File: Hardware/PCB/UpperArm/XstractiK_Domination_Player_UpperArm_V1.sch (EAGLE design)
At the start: 57 parts, among them J1 USB4110-GF-A_REVB, Q1 MMBT2222, Q2 AO3401A, Q5 MMBT2222, Q6 MMBT2222, U1 ESP32-DEVKITC-32U, U2 RFM95W-915S2, U3 MCP73831T, U4 AP2112K-3.3, U5 MAX17048G, U6 ESP32-WROOM-32D, U7 CH340C, U8 DS3231SN, U9 QMC5883GY-271

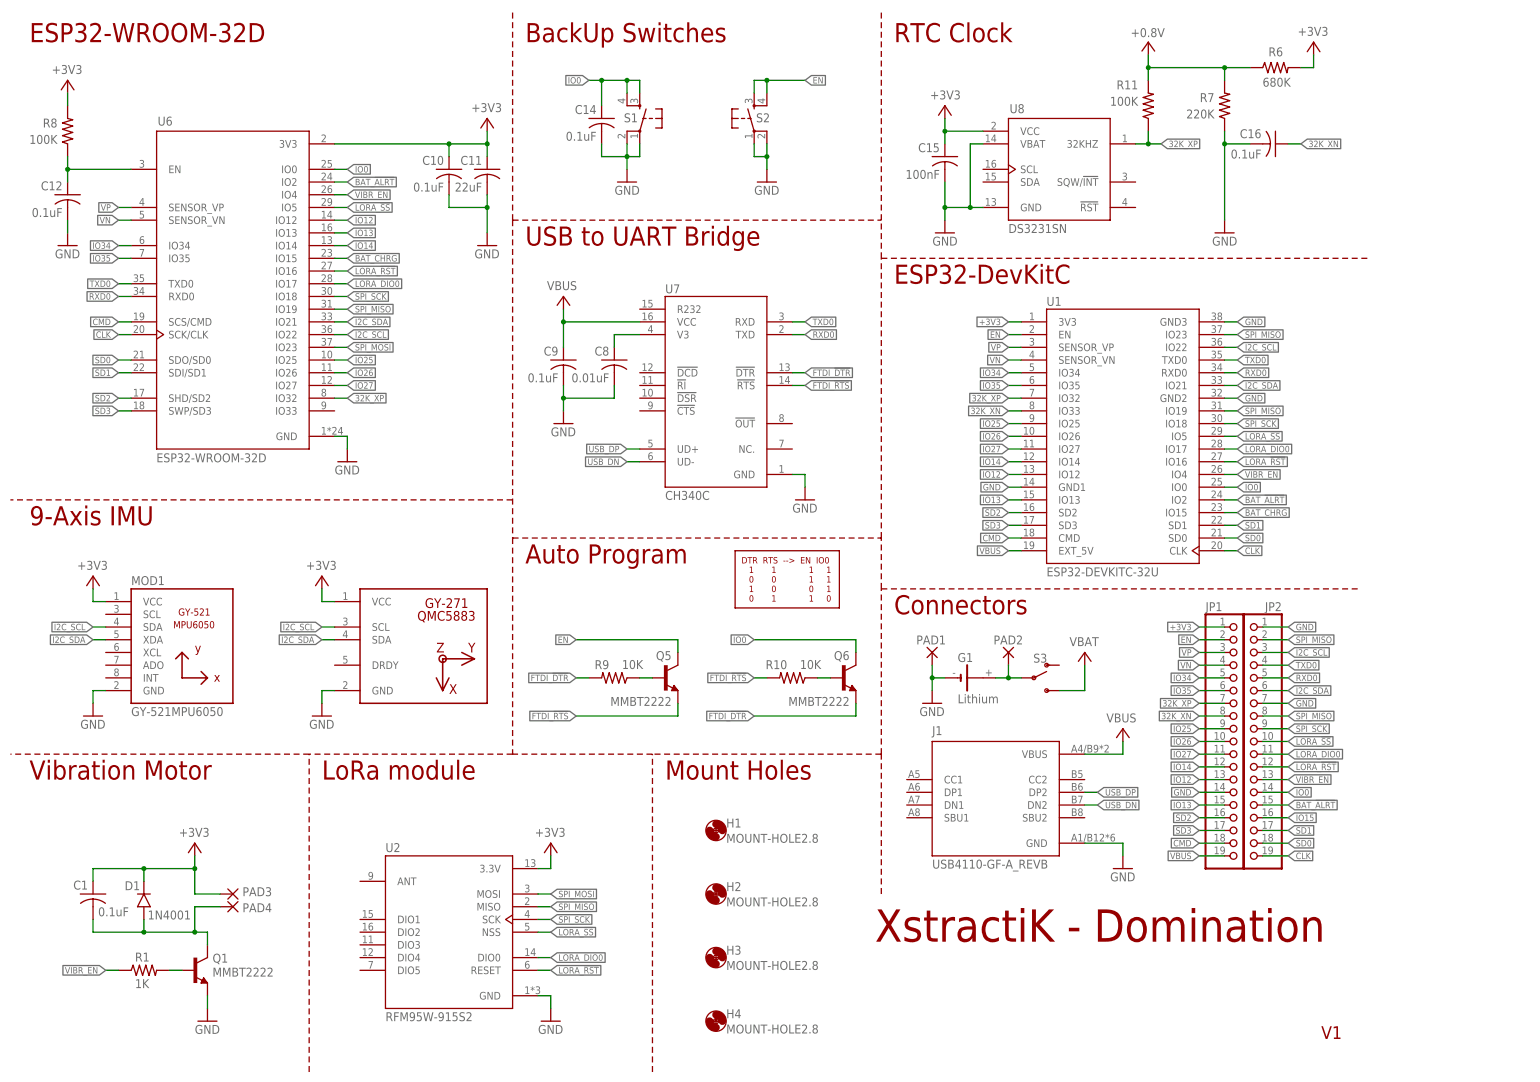
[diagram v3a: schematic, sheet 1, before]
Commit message: Schematic and PCB
UpperArm and Forearm designs
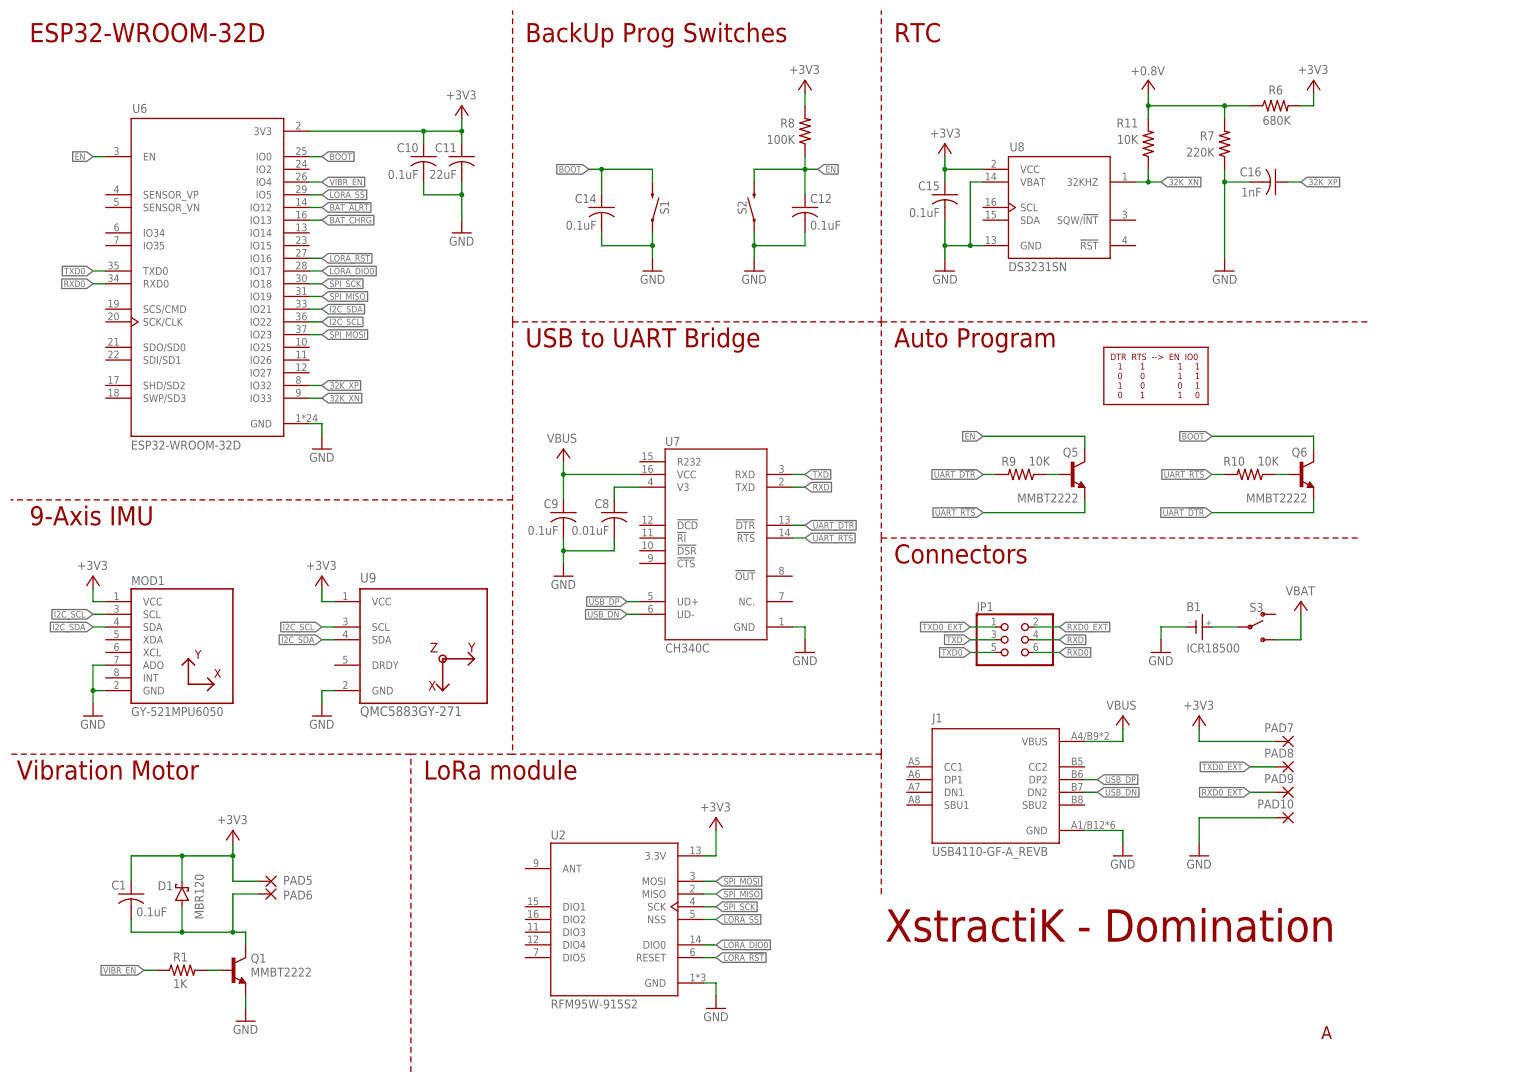
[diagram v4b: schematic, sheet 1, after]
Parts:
- removed G1: Lithium, battery:CR-AA
- removed H1, H2, H3, H4: MOUNT-HOLE2.8, holes:MOUNT-HOLE2.8
- removed JP2: (no value), pinhead:PINHD-1X19
- removed PAD1, PAD2, PAD3, PAD4: (no value), wirepad:SMD5
- removed U1: ESP32-DEVKITC-32U, ESP32-DEVKITC-32U:ESP32-DEVKITC-32U
- added B1: ICR18500, Batteries:ICR18500
- added PAD10, PAD7, PAD8, PAD9: WIREPADSMD1,27-254, wirepad:WIREPADSMD1,27-254
- added PAD5, PAD6: WIREPAD1,6/0,8, wirepad:WIREPAD1,6/0,8
- C15: value 100nF -> 0.1uF
- C16: value 0.1uF -> 1nF
- D1: value 1N4001 -> ON_SEMICONDUCTOR_MBR120VLSFT1GON_SEMICONDUCTOR_MBR120VLSFT1G_0_0; device 1N4001:1N4001 -> MBR120VLSFT1G:ON_SEMICONDUCTOR_MBR120VLSFT1GON_SEMICONDUCTOR_MBR120VLSFT1G_0_0
- JP1: device pinhead:PINHD-1X19 -> pinhead:PINHD-2X3
- R11: value 100K -> 10K
- S1, S2: value (none) -> MOMENTARY-SWITCH-SPST-SMD-5.2MM-TALL; device Switches:MOMENTARY-SWITCH-SPST-2-SMD-5.2MM -> Switches:MOMENTARY-SWITCH-SPST-SMD-5.2MM-TALL
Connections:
- net FTDI_!DTR renamed UART_!DTR
- net FTDI_!RTS renamed UART_!RTS
- net N$3 renamed V3
- removed net CLK: JP2.19, U1.CLK, U6.SCK/CLK
- removed net CMD: JP1.18, U1.CMD, U6.SCS/CMD
- removed net IO0: C14.1, JP2.14, Q6.C, S1.3, S1.4, U1.IO0, U6.IO0
- removed net IO12: JP1.13, U1.IO12, U6.IO12
- removed net IO13: JP1.15, U1.IO13, U6.IO13
- removed net IO14: JP1.12, U1.IO14, U6.IO14
- removed net IO15: JP2.16
- removed net IO25: JP1.9, U1.IO25, U6.IO25
- removed net IO26: JP1.10, U1.IO26, U6.IO26
- removed net IO27: JP1.11, U1.IO27, U6.IO27
- removed net IO34: JP1.5, U1.IO34, U6.IO34
- removed net IO35: JP1.6, U1.IO35, U6.IO35
- removed net LORA_!SS: JP2.10, U1.IO5, U2.NSS, U6.IO5
- removed net N$1: C1.2, D1.ANODE, PAD4.P, Q1.C
- removed net N$4: R4.1
- removed net N$8: G1.+, PAD2.P, S3.P
- removed net SD0: JP2.18, U1.SD0, U6.SDO/SD0
- removed net SD1: JP2.17, U1.SD1, U6.SDI/SD1
- removed net SD2: JP1.16, U1.SD2, U6.SHD/SD2
- removed net SD3: JP1.17, U1.SD3, U6.SWP/SD3
- removed net VCC: U9.VCC
- removed net VN: JP1.4, U1.SENSOR_VN, U6.SENSOR_VN
- removed net VP: JP1.3, U1.SENSOR_VP, U6.SENSOR_VP
- new net +: B1.+, S3.P
- new net +0.8V: R11.2, R6.1, R7.2
- new net -: B1.-
- new net BOOT: C14.1, Q6.C, S1.2, U6.IO0
- new net LORA_SS: U2.NSS, U6.IO5
- new net M-: C1.2, D1.A, PAD6.P, Q1.C
- new net RXD: JP1.4, U7.TXD
- new net RXD0_EXT: JP1.2, PAD9.P
- new net TXD: JP1.3, U7.RXD
- new net TXD0_EXT: JP1.1, PAD8.P
- net +3V3: now also D1.K, PAD5.P, PAD7.P, U9.VCC; no longer D1.CATHODE, JP1.1, PAD3.P, U1.3V3
- net 32K_XN: now also R11.1, U6.IO33, U8.32KHZ; no longer C16.1, JP1.8, U1.IO33
- net 32K_XP: now also C16.1; no longer JP1.7, R11.1, U1.IO32, U8.32KHZ
- net BAT_!ALRT: now also U6.IO12; no longer JP2.15, U1.IO2, U6.IO2
- net BAT_CHRG: now also U6.IO13; no longer U1.IO15, U6.IO15
- net EN: now also S2.2; no longer JP1.2, S2.3, S2.4, U1.EN
- net GND: now also MOD1.ADO, PAD10.P; no longer G1.-, JP1.14, JP2.1, JP2.7, PAD1.P, S1.2, S2.2, U1.GND1, U1.GND2, U1.GND3
- net I2C_SCL: now also MOD1.SCL; no longer JP2.3, MOD1.SDA, U1.IO22
- net I2C_SDA: now also MOD1.SDA; no longer JP2.6, MOD1.XDA, U1.IO21
- net LORA_!RST: no longer JP2.12, U1.IO16
- net LORA_DIO0: no longer JP2.11, U1.IO17
- net REG_VIN: now also R4.1
- net RXD0: now also JP1.6; no longer JP2.5, U1.RXD0, U7.TXD
- net SPI_MISO: no longer JP2.2, JP2.8, U1.IO19, U1.IO23
- net SPI_SCK: no longer JP2.9, U1.IO18
- net TXD0: now also JP1.5; no longer JP2.4, U1.TXD0, U7.RXD
- net VBUS: no longer JP1.19, R11.2, R6.1, R7.2, U1.EXT_5V
- net VIBR_EN: no longer JP2.13, U1.IO4
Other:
- note added: "A"
- note added: "BackUp Prog Switches"
- note added: "RTC"
- note removed: "BackUp Switches"
- note removed: "ESP32-DevKitC"
- note removed: "Mount Holes"
- note removed: "RTC Clock"
- note removed: "V1"
- moved on the sheet: C1, C10, C11, C12, C14, C15, C16, C8, C9, J1, Q1, Q5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
